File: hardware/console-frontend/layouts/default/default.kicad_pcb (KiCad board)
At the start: 2 copper layers, 100 x 100 mm, 45 parts

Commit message: FFCコネクタの並び順を変更(音声を1〜3番、映像を5〜9番へ)
ohnaka の指示(2026-09-22、レイアウト都合)。メイン基板 J15 の並びを:

    1 音声L / 2 GND / 3 音声R / 4 GND / 5 Pb / 6 GND / 7 C / 8 GND / 9 Y / 10 GND
    11 LED_DATA / 12 GPIO2 / 13 GPIO1(スイッチ選択) / 14 GND / 15 +3.3V / 16 +5V

小亀基板(J1)は type A・対向配置の前提で**逆順(n ↔ 17-n)**なので、そちらも
合わせて直した(1=+5V ... 8=Y / 10=C / 12=Pb / 14=音声R / 16=音声L)。
**片方だけ直すと全部ずれる。**

映像3本(Pb/C/Y)と音声2本は、いずれもGNDで挟まれたまま。

## 既存配線への影響(小亀基板)

FFCのピン割当が変わったため、ネット番号が振り直されて**13本の配線が消えた番号を
指す状態**になっていた(y_out / c_out / aud_l_out / aud_r_out)。旧ファイルの
番号→ネット名→新番号 で機械的に復元した(15箇所)。配線31本・ビア2本・
部品45個の位置は変わっていない。

残る食い違いは**2箇所だけ**で、旧ピンへ引いてあった音声の末端:

    aud_r_out の配線が y_out のパッドに乗っている  (138.25, 132.35)
    aud_l_out の配線が c_out のパッドに乗っている  (137.25, 132.35)

この2本は引き直しが要る(DRCで shorting_items として出る)。それ以外の
違反はシルクの重なりなど従来どおり。

Co-Authored-By: Claude Opus 5 (1M context) <noreply@anthropic.com>
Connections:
- J1 pad 10: aud_l_out -> c_out
- J1 pad 14: c_out -> aud_r_out
- J1 pad 16: y_out -> aud_l_out
- J1 pad 3: gpio2 -> gnd
- J1 pad 5: gnd -> gpio2
- J1 pad 8: aud_r_out -> y_out

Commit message: FFCコネクタを16芯から20芯に変更(全信号をGNDで挟み、電源を2本ずつに)
小亀基板(hardware/console-frontend)とメイン基板(hardware/adc-frontend)を
つなぐ0.5mmピッチFFCを HDGC 0.5K-1.5-16PWB (C2919558) から
0.5K-1.5-20PWB (C2919559) へ差し替えた。

16芯では制御3本(LED_DATA / GPIO2 / GPIO1)が隣り合っていて、800kHzで
たたく LED_DATA が GPIO と 10cm 並走していた。増やした4本を使って

  - LED_DATA / GPIO2 / GPIO1 のそれぞれにも GND を隣接させ、
    **全信号が両隣に GND を持つ**ようにした
  - +3.3V と +5V を2本ずつにして往復抵抗を半分にした

メイン基板 J15 の並び(小亀基板 J1 は type A FFC のため n ↔ 21-n の鏡像):

  音声L/GND/音声R/GND/Pb/GND/C/GND/Y/GND/
  LED/GND/GPIO2/GND/GPIO1/GND/+3.3V/+3.3V/+5V/+5V

両基板のフットプリントは tools/refresh_footprint.py で差し替え、配置
(メイン J15 = 126.4, 55.65 / 小亀 J1 = 138, 131, 180°)とデジグネータは
そのまま維持している。小亀基板の FFC 周辺の配線は ohnaka が引き直す。

Co-Authored-By: Claude Opus 5 (1M context) <noreply@anthropic.com>
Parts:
- J1: footprint HDGC_0_5K_1_5_16PWB:FPC-SMD_16P-P0.50_HDGC_0.5K-1.5-16PWB -> HDGC_0_5K_1_5_20PWB:FPC-SMD_20P-P0.50_HDGC_0.5K-1.5-20PWB
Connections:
- J1 pad 10: c_out -> led_din
- J1 pad 12: pb_out -> y_out
- J1 pad 14: aud_r_out -> c_out
- J1 pad 16: aud_l_out -> pb_out
- J1 pad 18: gnd -> aud_r_out
- J1 pad 2: p3v3 -> p5v
- J1 pad 3: gnd -> p3v3
- J1 pad 4: sw_sel -> p3v3
- J1 pad 5: gpio2 -> gnd
- J1 pad 6: led_din -> sw_sel
- J1 pad 8: y_out -> gpio2
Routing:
- net y_out: track 38.9 -> 0.00 mm
- net aud_r_out: track 40.9 -> 79.7 mm
- net pb_out: track 67.8 -> 103.3 mm
- net c_out: track 35.5 -> 0.00 mm

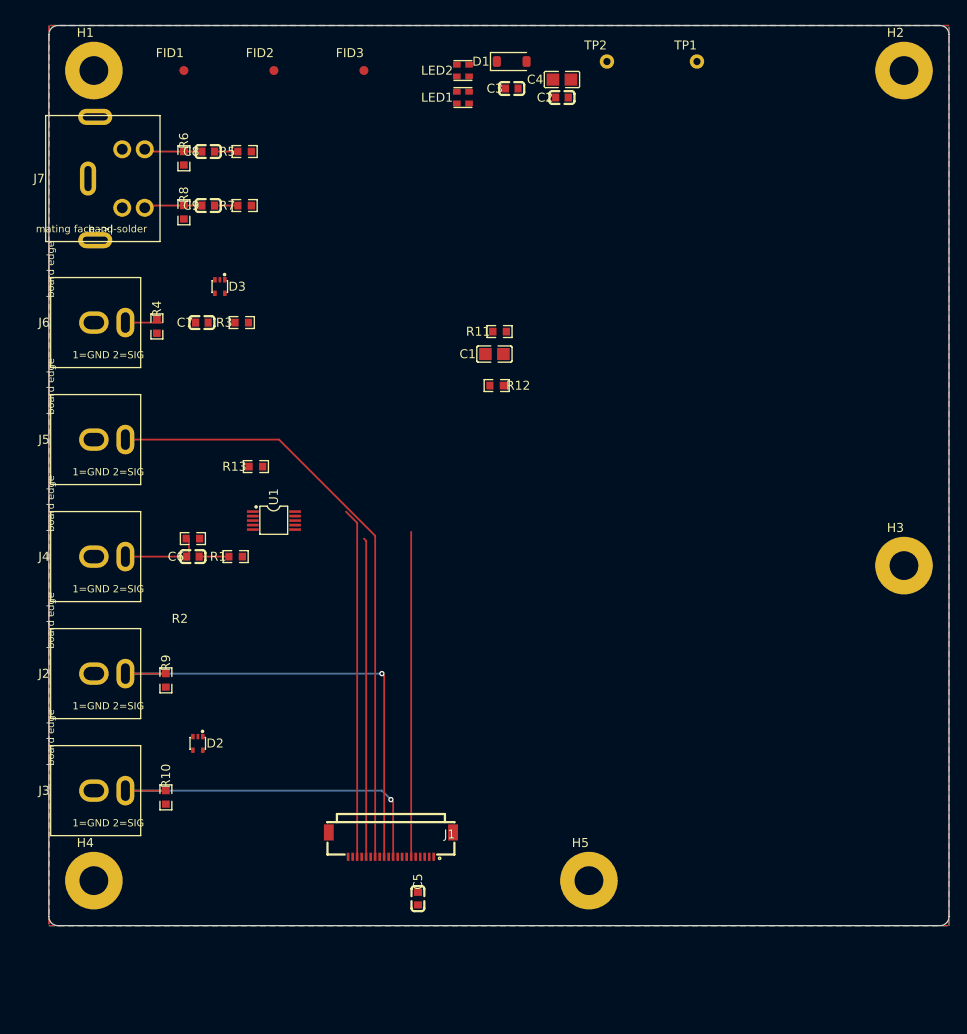
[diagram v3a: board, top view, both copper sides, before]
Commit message: PLR135/T10 のランドの向きを直す(取付穴が信号列の逆側だった)
取付穴は**信号列と光ポート開口部の「あいだ」**にある。信号列がいちばん奥で、
そこから +2.62mm が取付穴、+11.11mm が開口面。信号列の後ろには 2.39mm しか
胴体が無い。`PLR135_T10.kicad_mod` はこれを -2.62mm 側に描いていたので、
現物のポストが入らない。

    修正前  信号列 Y=0   取付穴 Y=-2.63   胴体 -3.85 .. +9.65   幅 8.60
    修正後  信号列 Y=0   取付穴 Y=+2.62   胴体 -2.39 .. +11.11  幅 9.70

`PLR135_T.kicad_mod`(v0.9.0 の /T 版)は取付穴を +3.95mm と正しく描けていた
ので、**/T10 を起こしたときに取付列だけ裏返った**もの。Kepler X
(`X68k-KeplerX-PCB` の U15 = `x68000-ext:XDCR_PLT133_T10W`)が同じランドを
持ち実基板で動いているので、寸法はそちらに合わせた。

取付穴が J8 pin1 の +2.62mm 側へ移った結果、**裏面の C77 と 0.052mm で
当たった**(取付穴は THT なので裏面にもランドが出る)。C77 を 1.2mm ずらし、
p3v3_spdif を取付穴の下を回るように引き直した。J8 の位置・信号3本の配線・
未配線0 はそのまま。

★**開口部は基板端から 2.46mm 張り出す。** 修正前は胴体を 9.65mm と短く
  描いていたので図面上は 1.0mm に見えていたが、現物は最初から 2.46mm 出る。
  ケースの開口はこの数字で合わせるか、J8 を内側へ寄せる。

## 文書のずれを訂正(ネットリストは正しく、文書だけが古かった)

- **FFC の逆順の式が 16芯時代の n↔17-n のまま**だった。20芯なので n↔21-n。
  `main.ato` 側は両基板とも 20本すべて正しい(1本ずつ照合済み)。
  小亀 README の ASCII 図と切り替え表は、さらに「音声を1〜3番、映像を5〜9番へ」
  の変更前の番号だった(Y=FFC1 等)。発注前チェックリストが誤った式で
  「確認せよ」と言う状態だったので直した
- レイアウト指示書のデジグネータ読み替え表が5行ずれていた(SO-DIMM /
  デジタルRGB端子 / MagJack / デジタルRGBバッファ / ESD)。
  **`.kicad_dru` の参照(U1 / U7 / U9 / JP1)は正しかった**ことを実体で確認済み
- ポゴピンを 4mm 品で確定(実測)。「自由長3mm・間隙2.6mm」の推定値を削除

## PCB(pcbnew での配置作業を含む)

    メイン基板  C7 / D10 の移動、J13 を 190.2 → 189.2
    小亀基板    SMD部品を裏面(B.Cu)へ移動し再配置

★メイン基板は**ゾーンの塗りが古い**。PWR層の p3v3_io と GND ビアが 0.000mm で
  当たり clearance / hole_clearance が 22件出ている。pcbnew で `B`(全ゾーン
  再塗り)を押すと全部消える(コピーで検証済み。未配線は 0 のまま)。

Co-Authored-By: Claude Opus 5 (1M context) <noreply@anthropic.com>
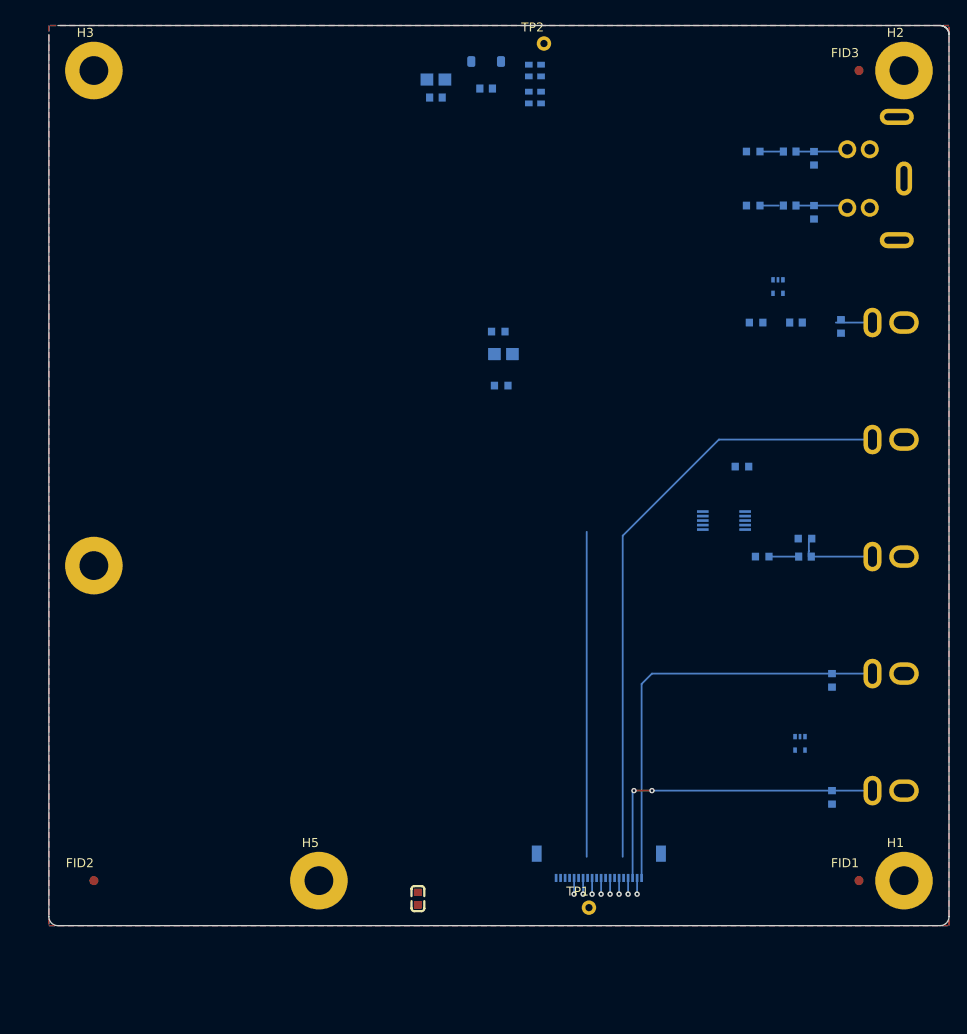
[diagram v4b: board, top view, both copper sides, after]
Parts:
- C1, C2, C3, C4, C6, C7, C8, C9, D1, D2, D3, H4, J1, J2, J3, J4, J5, J6, J7, LED1, LED2, R1, R10, R11, R12, R13, R2, R3, R4, R5, R6, R7, R8, R9, U1: moved to B.Cu
- moved H1 127.3 mm to (195.0, 135.0)
- moved FID1 117.2 mm to (190.0, 135.0)
- moved H3 105.5 mm to (105.0, 45.0)
- moved J7 100.0 mm to (199.7, 57.0), turned to 180 degrees
- moved J2 99.6 mm to (199.8, 112.0), turned to 180 degrees
- moved J3 99.6 mm to (199.8, 125.0), turned to 180 degrees
- moved J4 99.6 mm to (199.8, 99.0), turned to 180 degrees
- moved J5 99.6 mm to (199.8, 86.0), turned to 180 degrees
- moved J6 99.6 mm to (199.8, 73.0), turned to 180 degrees
- moved TP1 94.8 mm to (160.0, 138.0)
- moved FID2 92.2 mm to (105.0, 135.0)
- moved R4 76.0 mm to (188.0, 73.4)
- moved R10 74.0 mm to (187.0, 125.8)
- moved R9 74.0 mm to (187.0, 112.8)
- moved R6 70.0 mm to (185.0, 54.8)
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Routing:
- net aud_r_out: track 79.7 -> 36.3 mm, vias 1 -> 2
- net pb_out: track 103.3 -> 67.8 mm
- net gnd: track 0.00 -> 14.4 mm, vias 0 -> 8
- net aud_l_out: track 53.5 -> 47.7 mm, vias 1 -> 0

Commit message: 小亀基板のシリアルLEDを WS2812B-2020-V6 ×4 にする
- メイン基板と同じ Worldsemi WS2812B-2020-V6(C52917434)に替え、
  VDD を FFC の +3.3V に直結。降圧用の 1N4148W(D1)を外した(D1 は欠番)
- LED を2個から4個に増やした。データは LED1→LED2→LED3→LED4 の直列で、
  未実装テストパッド(TP2)は LED4 の DO に付け替えた
- 各 LED に 100nF(C2/C3/C10/C11)、LED 群の入口に 10µF(C4)。
  4個全白で約150mA。中点バイアスは 5kΩ×10µF で切ってあるので
  2kHz の PWM リップルはほぼ通らない
- ★MSL 5a。JLCPCB の焼成(追加料金)が要る
- 基板には GUI での手作業の配置・配線の変更も含む
- README と layout-guidelines の LED の記述を更新

Co-Authored-By: Claude Opus 5.5 (1M context) <noreply@anthropic.com>
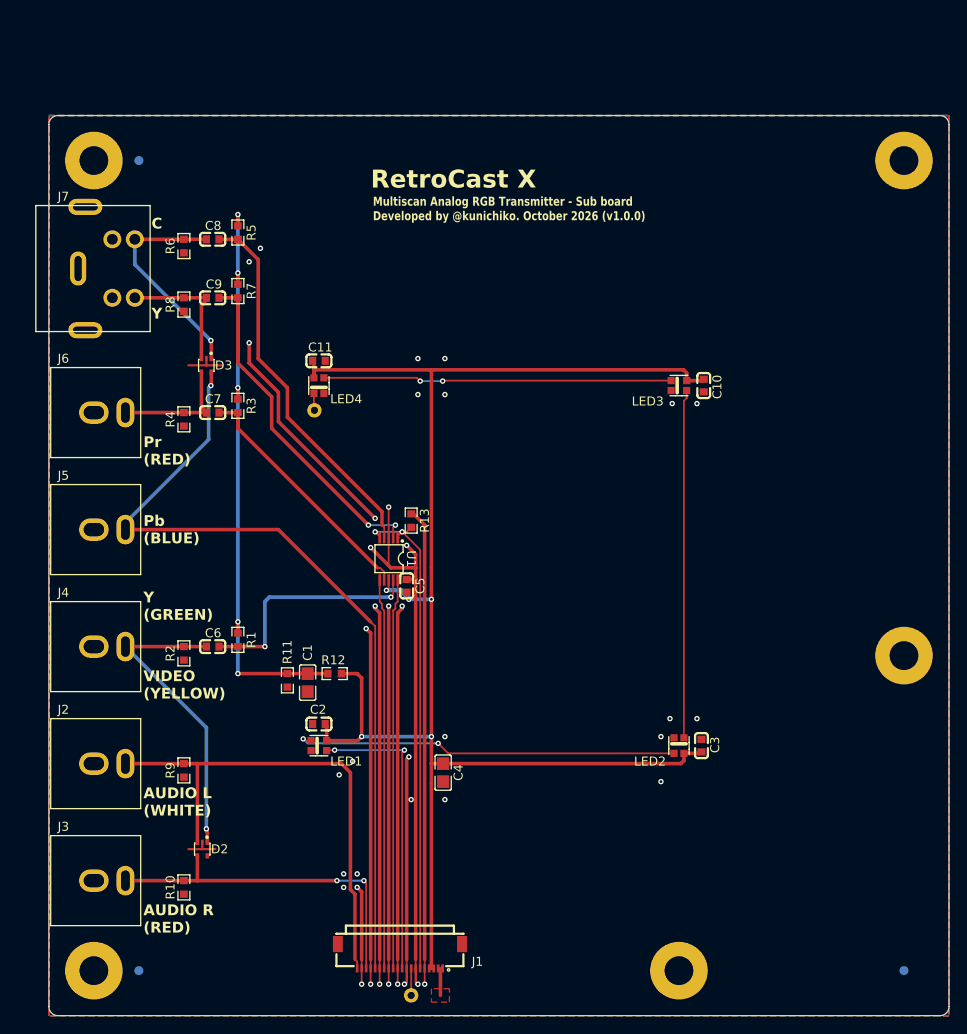
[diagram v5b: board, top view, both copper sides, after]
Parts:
- removed D1: , ST_1N4148W:D_SOD-123
- added C10: 100nF ±10%, YAGEO_CC0603KRX7R9BB104:C0603, F.Cu at (172.8, 80.0)
- added C11: 100nF ±10%, YAGEO_CC0603KRX7R9BB104:C0603, F.Cu at (130.0, 77.2)
- added LED3: , worldsemi_WS2812B_2020_V6:LED-SMD_4P-L2.2-W2.0-P1.00_WS2815C-2020-4P, F.Cu at (170.0, 80.0)
- added LED4: , worldsemi_WS2812B_2020_V6:LED-SMD_4P-L2.2-W2.0-P1.00_WS2815C-2020-4P, F.Cu at (130.0, 80.0)
- C1, C2, C3, C4, C6, C7, C8, C9, D2, D3, H4, J1, J2, J3, J4, J5, J6, J7, R1, R10, R11, R12, R13, R2, R3, R4, R5, R6, R7, R8, R9, U1: moved to F.Cu
- FID1, FID2, FID3, H1, H2, H3, H5, TP1, TP2: moved to B.Cu
- LED1, LED2: footprint XINGLIGHT_XL_2020RGBC_2812B:LED-SMD_4P-L2.0-W2.0-BR-1 -> worldsemi_WS2812B_2020_V6:LED-SMD_4P-L2.2-W2.0-P1.00_WS2815C-2020-4P; moved to F.Cu
- moved J7 101.6 mm to (98.5, 67.0), turned to 0 degrees
- moved J2 100.1 mm to (100.2, 122.0), turned to 0 degrees
- moved J3 100.1 mm to (100.2, 135.0), turned to 0 degrees
- moved J4 100.1 mm to (100.2, 109.0), turned to 0 degrees
- moved J5 100.1 mm to (100.2, 96.0), turned to 0 degrees
- moved J6 100.1 mm to (100.2, 83.0), turned to 0 degrees
- moved FID2 90.6 mm to (195.0, 145.0), turned to 180 degrees
- moved H1 90.6 mm to (105.0, 145.0), turned to 180 degrees
- moved H2 90.6 mm to (105.0, 55.0), turned to 180 degrees
- moved H3 90.6 mm to (195.0, 55.0), turned to 180 degrees
- moved H4 90.6 mm to (195.0, 110.0), turned to 0 degrees
- moved FID1 80.6 mm to (110.0, 145.0), turned to 180 degrees
- moved FID3 80.6 mm to (110.0, 55.0), turned to 180 degrees
- moved C4 77.0 mm to (143.8, 123.0), turned to -90 degrees
- moved C3 76.8 mm to (172.5, 120.0), turned to 90 degrees
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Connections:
- C2 pad 1: p_led_4v3 -> p3v3
- C3 pad 1: p_led_4v3 -> p3v3
- C4 pad 1: p_led_4v3 -> p3v3
- LED1 pad 4: p_led_4v3 -> p3v3
- LED2 pad 4: p_led_4v3 -> p3v3
- TP2 pad 1: led2_dout -> led4_dout
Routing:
- net gnd: track 14.4 -> 355.7 mm, vias 8 -> 39
- net p3v3: track 0.00 -> 178.2 mm, vias 0 -> 5
- net vbias_1v65: track 0.00 -> 66.0 mm, vias 0 -> 5
- net c_out: track 0.00 -> 43.4 mm
- net y_out: track 0.00 -> 43.4 mm
- net led1_dout: track 0.00 -> 42.8 mm, vias 0 -> 2
- net sv_c_ac: track 2.60 -> 42.0 mm
- net led3_dout: track 0.00 -> 38.7 mm, vias 0 -> 2
- net led2_dout: track 0.00 -> 38.7 mm
- net sv_y_ac: track 2.16 -> 37.9 mm, vias 0 -> 2
- net led_din: track 0.00 -> 33.0 mm, vias 0 -> 2
- net pr_ac: track 0.00 -> 27.6 mm
- net cvbs_in: track 9.08 -> 34.5 mm, vias 0 -> 1
- net pb_out: track 67.8 -> 91.7 mm, vias 0 -> 1
- net cvbs_ac: track 3.30 -> 26.3 mm, vias 0 -> 2
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- added copper zone on F.Cu, net p5v
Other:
- board text added: "${TITLE}"
- board text added: "AUDIO L (WHITE)"
- board text added: "AUDIO R (RED)"
- board text added: "C"
- board text added: "Multiscan Analog RGB Transmitter - Sub board Developed by @kunichiko. October 2026 (${REVISION})"
- board text added: "Pb (BLUE)"
- board text added: "Pr (RED)"
- board text added: "VIDEO (YELLOW)"
- board text added: "Y"
- board text added: "Y (GREEN)"
